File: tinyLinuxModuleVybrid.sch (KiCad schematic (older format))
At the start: 46 parts, among them M102 SCREW, M104 SCREW, M106 SCREW, M108 SCREW, Q101 2N7002BKT, Q102 2N7002BKT, Q103 2N7002BKT, X101 MICROSD, X102 LAN_Transformer, X103 CONN_01x06, X104 VybridBoard, X105 ARM_JTAG_10

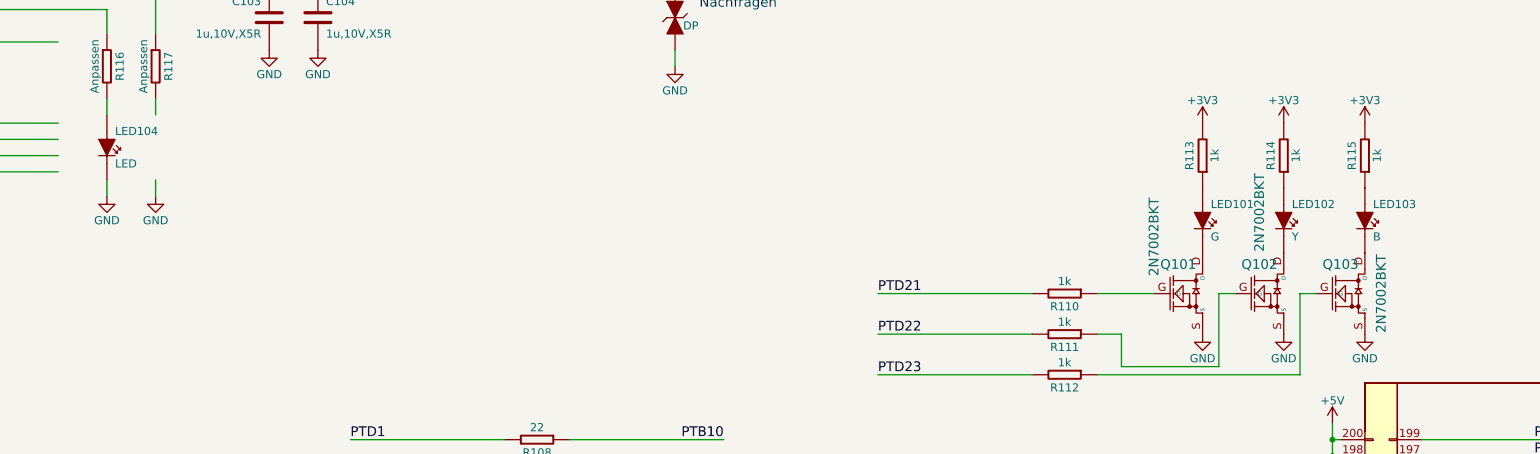
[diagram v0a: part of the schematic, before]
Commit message: adjusted power supply and sensors
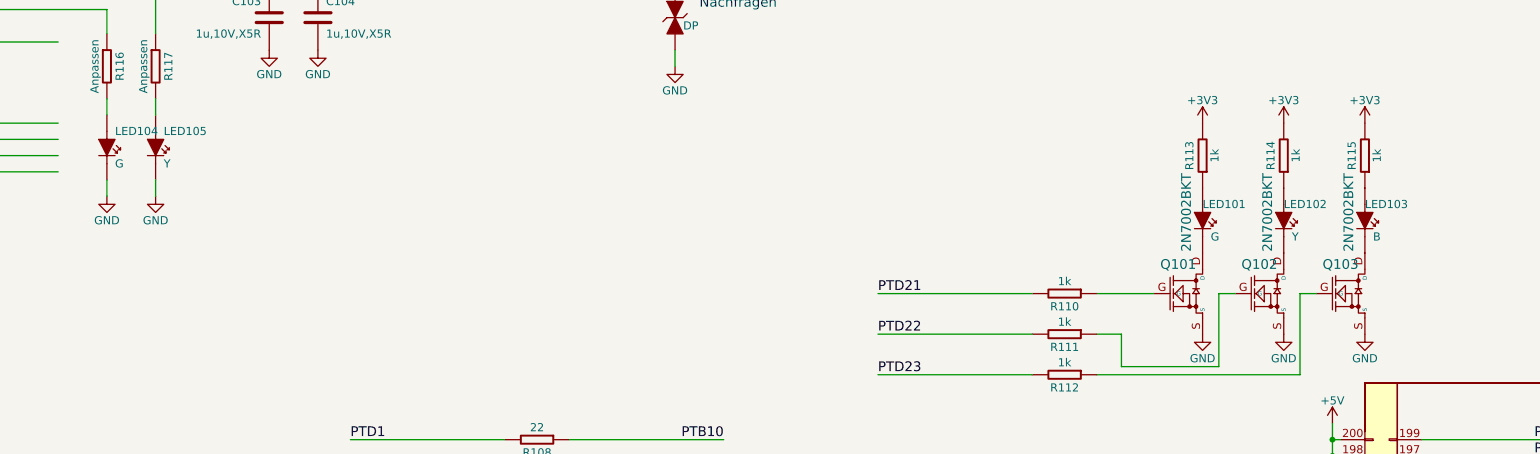
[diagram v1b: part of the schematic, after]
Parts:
- added LED105: Y, Passives:LED0603N, symbol LED
- LED104: value LED -> G; footprint (none) -> Passives:LED0603N
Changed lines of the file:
@@
 U 1 1 562E5AB9
 P 10850 3150
-F 0 "LED101" H 10900 3250 50  0000 L CNN
+F 0 "LED101" H 10850 3250 50  0000 L CNN
 F 1 "G" H 10900 3050 50  0000 L CNN
 F 2 "Passives:LED0603N" H 10888 3000 30  0001 C CNN
@@
 U 1 1 562E5DDD
 P 11350 3150
-F 0 "LED102" H 11400 3250 50  0000 L CNN
+F 0 "LED102" H 11350 3250 50  0000 L CNN
 F 1 "Y" H 11400 3050 50  0000 L CNN
 F 2 "Passives:LED0603N" H 11388 3000 30  0001 C CNN
@@
 U 1 1 562E5EE3
 P 11850 3150
-F 0 "LED103" H 11900 3250 50  0000 L CNN
+F 0 "LED103" H 11850 3250 50  0000 L CNN
 F 1 "B" H 11900 3050 50  0000 L CNN
 F 2 "Passives:LED0603N" H 11888 3000 30  0001 C CNN
@@
 P 10850 3600
 F 0 "Q101" H 10700 3780 60  0000 C CNN
-F 1 "2N7002BKT" V 10550 3950 60  0000 C CNN
+F 1 "2N7002BKT" V 10750 4100 60  0000 C CNN
 F 2 "Transistor:SOT416_GSD" H 10200 3925 60  0001 C CNN
 F 3 "" H 10200 3925 60  0000 C CNN
@@
 P 11350 3600
 F 0 "Q102" H 11200 3780 60  0000 C CNN
-F 1 "2N7002BKT" V 11200 4100 60  0000 C CNN
+F 1 "2N7002BKT" V 11250 4100 60  0000 C CNN
 F 2 "Transistor:SOT416_GSD" H 10700 3925 60  0001 C CNN
 F 3 "" H 10700 3925 60  0000 C CNN
@@
 P 11850 3600
 F 0 "Q103" H 11700 3780 60  0000 C CNN
-F 1 "2N7002BKT" V 11950 3600 60  0000 C CNN
+F 1 "2N7002BKT" V 11750 4100 60  0000 C CNN
 F 2 "Transistor:SOT416_GSD" H 11200 3925 60  0001 C CNN
 F 3 "" H 11200 3925 60  0000 C CNN
@@
 P 4100 2700
 F 0 "LED104" H 4150 2800 50  0000 L CNN
-F 1 "LED" H 4150 2600 50  0000 L CNN
-F 2 "" H 4138 2550 30  0000 C CNN
+F 1 "G" H 4150 2600 50  0000 L CNN
+F 2 "Passives:LED0603N" H 4138 2550 30  0001 C CNN
 F 3 "" H 4100 2700 60  0000 C CNN
 	1    4100 2700
@@
 Text Notes 7750 1850 0    60   ~ 0
 Nachfragen
+$Comp
+L LED LED105
+U 1 1 572A04C6
+P 4400 2700
+F 0 "LED105" H 4450 2800 50  0000 L CNN
+F 1 "Y" H 4450 2600 50  0000 L CNN
+F 2 "Passives:LED0603N" H 4438 2550 30  0001 C CNN
+F 3 "" H 4400 2700 60  0000 C CNN
+	1    4400 2700
+	1    0    0    -1
+$EndComp
 $EndSCHEMATC

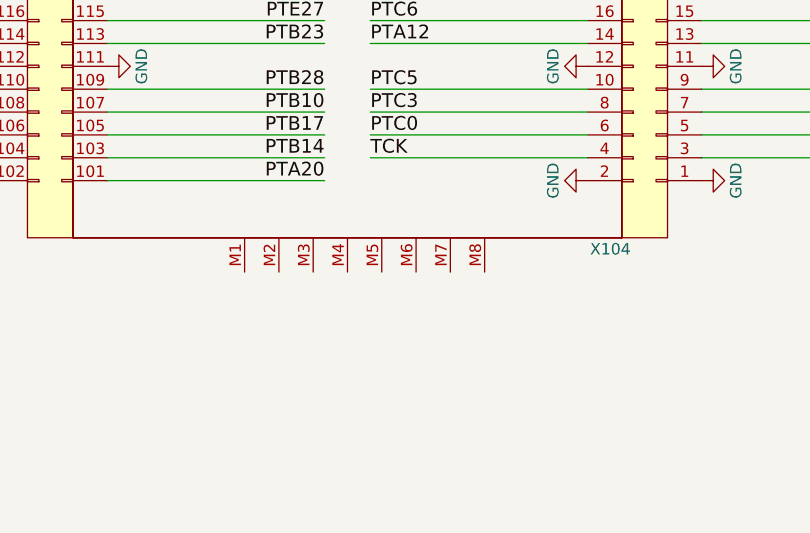
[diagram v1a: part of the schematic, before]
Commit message: adjusted 3d models
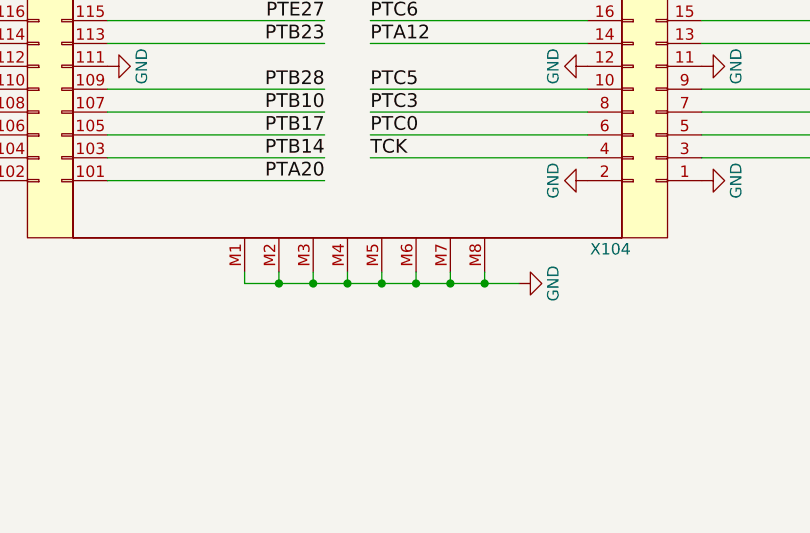
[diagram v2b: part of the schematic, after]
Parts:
- X103: footprint Connector:MLX127_53398_SMD-06 -> Connector:PicoLock_6
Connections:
- wire segments 280 -> 289

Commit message: sorted components
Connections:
- wire segments 289 -> 305
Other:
- note added: "Funktion!"
- note added: "Was ist das?"
- moved on the sheet: X103

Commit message: sorted components
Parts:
- removed R108, R109: 22, Passives:R0402N, symbol R
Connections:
- wire segments 305 -> 302
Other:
- note added: "???"
- note removed: "Was ist das?"
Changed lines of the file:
@@
 Text Label 600  8750 0    60   ~ 0
 PTB20
-Text Label 7900 4500 2    60   ~ 0
-PTB10
 Text Label 600  9350 0    60   ~ 0
 PTB28
@@
 Text Label 600  9750 0    60   ~ 0
 PTC27
-Text Label 7900 4750 2    60   ~ 0
-PTB11
 Text Label 600  8950 0    60   ~ 0
 PTB22
@@
 F26 "USBD_D+" I R 2900 2750 60
 F27 "USBD_D-" I R 2900 2850 60
+F28 "RX_NEO" I L 1300 1000 60
+F29 "TX_NEO" I L 1300 1150 60
 $EndSheet
 $Comp
@@
 	600  8950 1550 8950
 Wire Wire Line
-	7900 4750 6950 4750
-Wire Wire Line
 	1550 9750 600  9750
 Wire Wire Line
@@
 	1550 9350 600  9350
 Wire Wire Line
-	7900 4500 6950 4500
-Wire Wire Line
 	1550 8750 600  8750
 Wire Wire Line
@@
 Wire Wire Line
 	600  9450 1550 9450
-Wire Wire Line
-	5600 4500 6550 4500
 Wire Wire Line
 	1550 10050 600  10050
@@
 Text Label 10750 5200 0    60   ~ 0
 PTE5
-$Comp
-L R R108
-U 1 1 56447E61
-P 6750 4500
-F 0 "R108" V 6830 4500 50  0000 C CNN
-F 1 "22" V 6675 4500 50  0000 C CNN
-F 2 "Passives:R0402N" V 6680 4500 30  0001 C CNN
-F 3 "" H 6750 4500 30  0000 C CNN
-	1    6750 4500
-	0    1    1    0
-$EndComp
-$Comp
-L R R109
-U 1 1 5644867F
-P 6750 4750
-F 0 "R109" V 6830 4750 50  0000 C CNN
-F 1 "22" V 6675 4750 50  0000 C CNN
-F 2 "Passives:R0402N" V 6680 4750 30  0001 C CNN
-F 3 "" H 6750 4750 30  0000 C CNN
-	1    6750 4750
-	0    1    1    0
-$EndComp
 $Comp
 L FIDUCIAL FID101
@@
 Wire Wire Line
 	8400 1350 8400 1400
-Text Notes 6500 4350 0    60   ~ 0
-Was ist das?
 Text Notes 12000 3350 0    60   ~ 0
 Funktion!
+Text Notes 3650 2000 0    60   ~ 0
+???
 $EndSCHEMATC

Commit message: selected connector pins
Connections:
- wire segments 302 -> 401
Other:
- note added: "CAN_0"
- note added: "I2C_0"
- note added: "I2C_1"
- note added: "INT ???"
- note added: "Platine"
- note added: "SPI_0"
- note added: "SPI_3"
- note added: "Sesnor Platine"
- note added: "Stecker"
- note added: "TD9 auf anderem Stecker, \nZeit Probleme"
- note added: "UART_1"
- note added: "UART_3"
- note added: "USB_1"
- note added: "VBUS braucht man das?\nVBUS_EN/OC was ist damit?"
- note added: "Was ist RTS,CTS?\nBraucht man das?"
- note removed: "???"

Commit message: stecker hinzugefügt
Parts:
- removed D101: DP, Passives:D_0402, symbol DP
- removed R116, R117: Anpassen, Passives:R0402N, symbol R
- removed R118, R119, R120, R121: 75, Passives:R0402N, symbol R
- added X106: CONN_02x50, Connector:ERF8-50-05.0-L-DV-K-TR, symbol CONN_02x50
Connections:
- net labels added: USBC_D+, USBC_D-, USBD_D+, USBD_D-
- wire segments 401 -> 378
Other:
- note added: "18+2(I2C)\n"
- note added: "6\n"
- note added: "8+8+6+20+4(PowerSuplly)=46\n"
- note added: "8\n"
- note added: "Wird schon benutzt anderen suchen\n"
- note removed: "Platine"
- note removed: "TD9 auf anderem Stecker, \nZeit Probleme"
- note removed: "Was ist RTS,CTS?\nBraucht man das?"
